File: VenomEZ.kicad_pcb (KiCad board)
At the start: 2 copper layers, 72 x 42 mm, 43 parts, among them CN1 HC-XH-5A-G, CN10 HC-XH-2A-G, CN2 HC-PH-8A-G, CN3 HC-XH-8A-G, CN4 HC-XH-8A-G, CN5 HC-XH-2A-G, CN6 HC-PH-7A-G, CN7 HC-XH-2A-G, CN8 HC-XH-2A-G, CN9 HC-XH-2A-G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

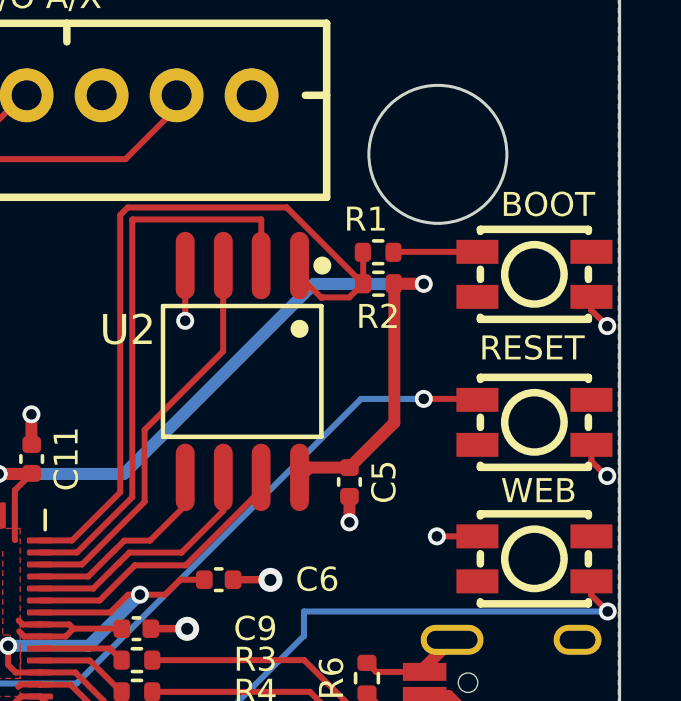
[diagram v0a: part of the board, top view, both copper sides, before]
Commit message: Move buttons and R1/R2 for better clearance around screw
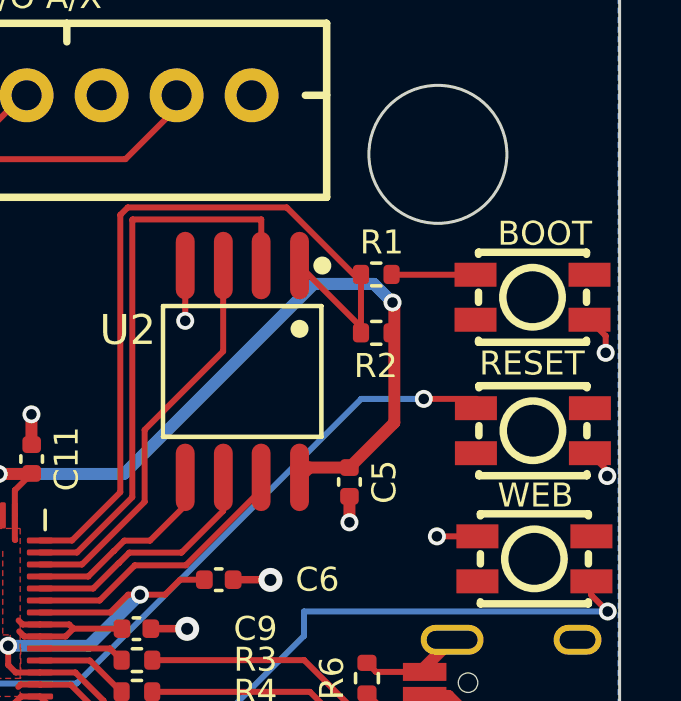
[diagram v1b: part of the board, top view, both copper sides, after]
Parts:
- moved R2 1.64 mm to (141.3, 86.7)
- moved SW3 0.77 mm to (146.6, 85.5)
- moved R1 0.74 mm to (141.3, 84.7)
- moved SW2 0.28 mm to (146.6, 89.9)
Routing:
- net +3V3: track 71.6 -> 69.2 mm
- net QSPI_SS: track 25.9 -> 26.5 mm

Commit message: 1.2
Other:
- board text added: "Version 1.2 Powered by GP2040-CE"
- board text removed: "Version 1.1 Powered by GP2040-CE"
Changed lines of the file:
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@@
     (effects (font (size 0.8 0.8) (thickness 0.15)) (justify left bottom))
   )
-  (gr_text "Version 1.1\nPowered by GP2040-CE" (at 96.396823 90.614668) (layer "F.SilkS")
+  (gr_text "Version 1.2\nPowered by GP2040-CE" (at 96.396823 90.614668) (layer "F.SilkS")
     (effects (font (size 1 1) (thickness 0.09)) (justify left bottom))
   )

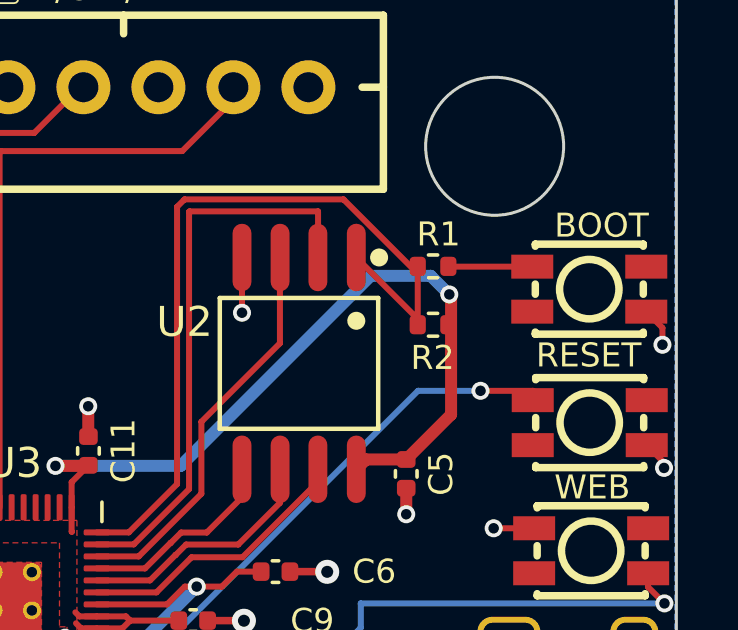
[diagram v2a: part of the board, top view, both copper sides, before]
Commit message: Move R1 and R2 closer together
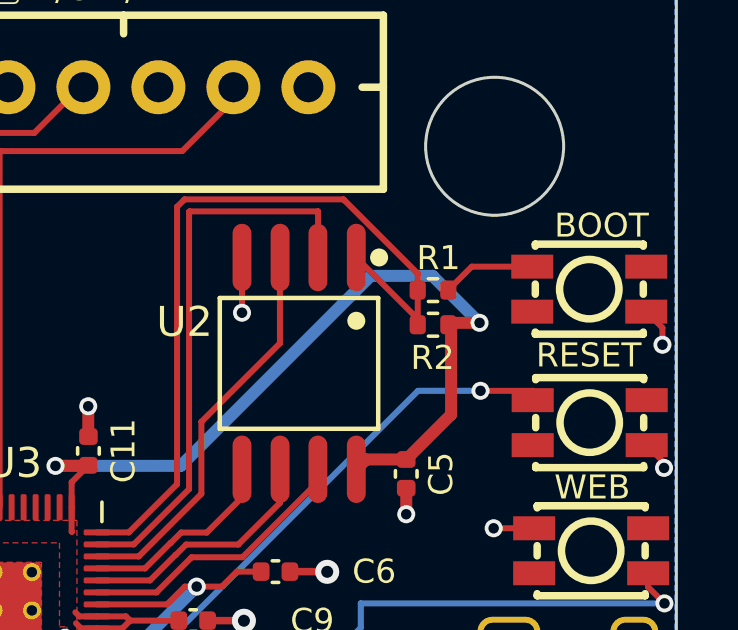
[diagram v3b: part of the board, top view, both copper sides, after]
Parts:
- moved R1 0.79 mm to (141.3, 85.5)
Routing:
- net +3V3: track 69.2 -> 70.7 mm
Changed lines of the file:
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@@
   )
   (footprint "Resistor_SMD:R_0402_1005Metric" (layer "F.Cu")
-    (at 141.348354 84.711995)
+    (at 141.347237 85.502328)
     (descr "Resistor SMD 0402 (1005 Metric), square (rectangular) end terminal, IPC_7351 nominal, (Body size source: IPC-SM-782 page 72, https://www.pcb-3d.com/wordpress/wp-content/uploads/ipc-sm-782a_amendment_1_and_2.pdf), generated with kicad-footprint-generator")
     (tags "resistor")
@@
   (segment (start 129.30151 98.990949) (end 129.512459 98.78) (width 0.2) (layer "F.Cu") (net 34))
   (segment (start 129.30151 93.552748) (end 129.313254 93.564492) (width 0.2) (layer "F.Cu") (net 34))
-  (segment (start 141.950201 85.707586) (end 141.890251 85.647636) (width 0.4) (layer "F.Cu") (net 34))
   (segment (start 129.844008 91.362421) (end 129.861793 91.344636) (width 0.2) (layer "F.Cu") (net 34))
   (segment (start 129.30151 92.7425) (end 129.30151 91.904919) (width 0.2) (layer "F.Cu") (net 34))
@@
   (segment (start 130.13901 98.38) (end 130.145139 98.386129) (width 0.2) (layer "F.Cu") (net 34))
   (segment (start 131.113273 96.38) (end 130.13901 96.38) (width 0.2) (layer "F.Cu") (net 34))
+  (segment (start 140.454685 91.148537) (end 141.950201 89.653021) (width 0.4) (layer "F.Cu") (net 34))
   (segment (start 129.30151 99.6175) (end 129.30151 98.990949) (width 0.2) (layer "F.Cu") (net 34))
   (segment (start 134.847542 106.924702) (end 135.041033 106.924702) (width 0.4) (layer "F.Cu") (net 34))
+  (segment (start 141.950201 89.653021) (end 141.950201 86.749551) (width 0.4) (layer "F.Cu") (net 34))
   (segment (start 129.30151 92.7425) (end 129.30151 93.552748) (width 0.2) (layer "F.Cu") (net 34))
   (segment (start 125.70151 92.7425) (end 125.70151 91.022448) (width 0.2) (layer "F.Cu") (net 34))
@@
   (segment (start 129.512459 98.78) (end 130.13901 98.78) (width 0.2) (layer "F.Cu") (net 34))
   (segment (start 122.05412 96.38) (end 123.26401 96.38) (width 0.2) (layer "F.Cu") (net 34))
-  (segment (start 141.950201 89.653021) (end 141.950201 85.707586) (width 0.4) (layer "F.Cu") (net 34))
   (segment (start 131.252393 96.51912) (end 130.991513 96.78) (width 0.2) (layer "F.Cu") (net 34))
   (segment (start 119.740309 106.064071) (end 120.28447 106.064071) (width 0.2) (layer "F.Cu") (net 34))
   (segment (start 135.057663 106.908072) (end 135.041033 106.924702) (width 0.2) (layer "F.Cu") (net 34))
   (segment (start 124.03519 96.38) (end 124.043381 96.388191) (width 0.2) (layer "F.Cu") (net 34))
+  (segment (start 141.922148 86.59391) (end 141.858354 86.657704) (width 0.4) (layer "F.Cu") (net 34))
   (segment (start 131.159352 98.386129) (end 131.857521 99.084298) (width 0.2) (layer "F.Cu") (net 34))
+  (segment (start 142.899201 86.59391) (end 141.922148 86.59391) (width 0.4) (layer "F.Cu") (net 34))
   (segment (start 131.857521 103.934681) (end 134.847542 106.924702) (width 0.4) (layer "F.Cu") (net 34))
   (segment (start 130.991513 96.78) (end 130.13901 96.78) (width 0.2) (layer "F.Cu") (net 34))
@@
   (segment (start 128.763082 91.362421) (end 129.844008 91.362421) (width 0.4) (layer "F.Cu") (net 34))
   (segment (start 131.857521 99.084298) (end 131.857521 100.711465) (width 0.2) (layer "F.Cu") (net 34))
+  (segment (start 141.950201 86.749551) (end 141.858354 86.657704) (width 0.4) (layer "F.Cu") (net 34))
   (segment (start 125.70151 99.6175) (end 125.70151 99.085025) (width 0.2) (layer "F.Cu") (net 34))
   (segment (start 129.617561 96.78) (end 129.446174 96.608613) (width 0.2) (layer "F.Cu") (net 34))
-  (segment (start 140.454685 91.148537) (end 141.950201 89.653021) (width 0.4) (layer "F.Cu") (net 34))
   (segment (start 130.13901 96.78) (end 129.617561 96.78) (width 0.2) (layer "F.Cu") (net 34))
   (segment (start 129.561589 96.38) (end 129.425324 96.243735) (width 0.2) (layer "F.Cu") (net 34))
   (segment (start 125.70151 91.022448) (end 125.43422 90.755158) (width 0.2) (layer "F.Cu") (net 34))
   (via (at 128.763082 91.362421) (size 0.6) (drill 0.35) (layers "F.Cu" "B.Cu") (free) (net 34))
-  (via (at 141.890251 85.647636) (size 0.6) (drill 0.35) (layers "F.Cu" "B.Cu") (free) (net 34))
+  (via (at 142.899201 86.59391) (size 0.6) (drill 0.35) (layers "F.Cu" "B.Cu") (free) (net 34))
   (segment (start 139.270815 85.027118) (end 132.935512 91.362421) (width 0.4) (layer "B.Cu") (net 34))
-  (segment (start 141.890251 85.647636) (end 141.269733 85.027118) (width 0.4) (layer "B.Cu") (net 34))
-  (segment (start 141.269733 85.027118) (end 139.270815 85.027118) (width 0.4) (layer "B.Cu") (net 34))
+  (segment (start 141.332409 85.027118) (end 139.270815 85.027118) (width 0.4) (layer "B.Cu") (net 34))
   (segment (start 132.935512 91.362421) (end 128.763082 91.362421) (width 0.4) (layer "B.Cu") (net 34))
+  (segment (start 142.899201 86.59391) (end 141.332409 85.027118) (width 0.4) (layer "B.Cu") (net 34))
   (segment (start 117.807657 95.133875) (end 118.253782 95.58) (width 0.2) (layer "F.Cu") (net 35))
   (segment (start 118.253782 95.58) (end 123.26401 95.58) (width 0.2) (layer "F.Cu") (net 35))
@@
   (segment (start 132.815831 82.727378) (end 132.815831 91.970701) (width 0.2) (layer "F.Cu") (net 42))
   (segment (start 131.206532 93.58) (end 130.13901 93.58) (width 0.2) (layer "F.Cu") (net 42))
-  (segment (start 144.656611 84.721509) (end 141.867868 84.721509) (width 0.2) (layer "F.Cu") (net 43))
-  (segment (start 141.867868 84.721509) (end 141.858354 84.711995) (width 0.2) (layer "F.Cu") (net 43))
+  (segment (start 142.638056 84.721509) (end 141.857237 85.502328) (width 0.2) (layer "F.Cu") (net 43))
+  (segment (start 144.656611 84.721509) (end 142.638056 84.721509) (width 0.2) (layer "F.Cu") (net 43))
   (segment (start 133.29924 94.408514) (end 132.127754 95.58) (width 0.2) (layer "F.Cu") (net 46))
   (segment (start 137.515259 91.890331) (end 134.997076 94.408514) (width 0.2) (layer "F.Cu") (net 46))

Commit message: Update silk for 1.3
(cherry picked from commit d50c346d8888544253aca363da94d46f0ae0f3f4)
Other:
- board text added: "Version 1.3 Powered by GP2040-CE"
- board text removed: "Version 1.2 Powered by GP2040-CE"
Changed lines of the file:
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@@
     (effects (font (size 0.8 0.8) (thickness 0.15)) (justify left bottom))
   )
-  (gr_text "Version 1.2\nPowered by GP2040-CE" (at 96.396823 90.614668) (layer "F.SilkS")
+  (gr_text "Version 1.3\nPowered by GP2040-CE" (at 96.396823 90.614668) (layer "F.SilkS")
     (effects (font (size 1 1) (thickness 0.09)) (justify left bottom))
   )

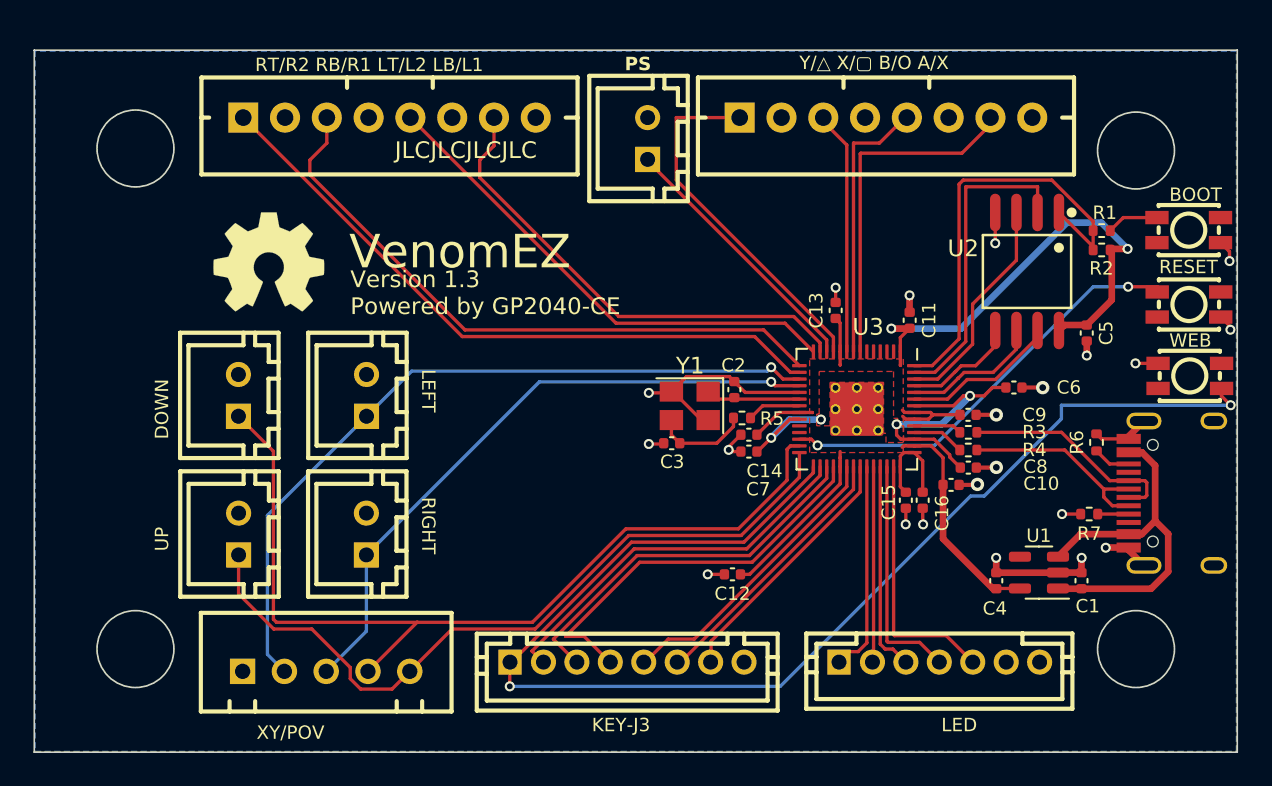
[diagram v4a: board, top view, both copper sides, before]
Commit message: Started og usb connector / redesign
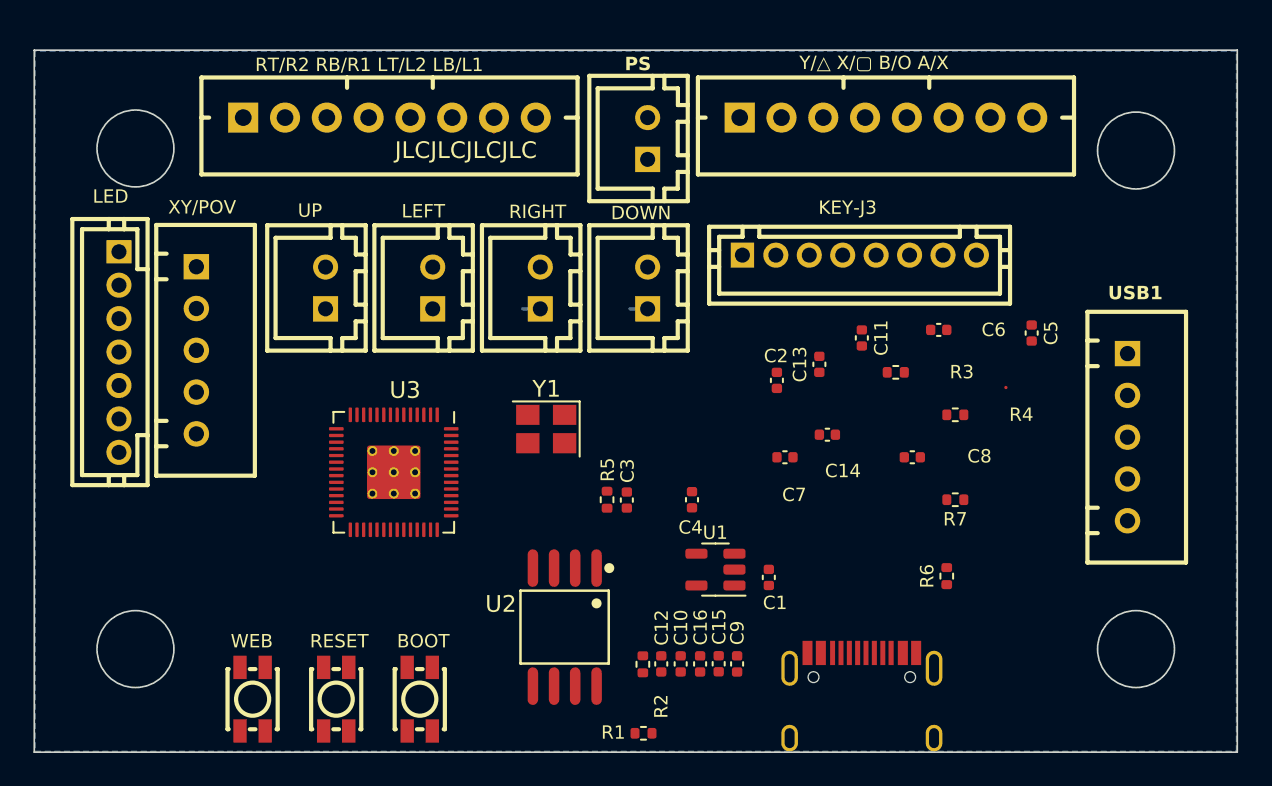
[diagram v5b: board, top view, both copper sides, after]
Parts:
- removed OSHW1: OSHW-Symbol_6.7x6mm_SilkScreen, Symbol:OSHW-Symbol_6.7x6mm_SilkScreen
- added CN11: HC-XH-5A-G, easyeda2kicad:CONN-TH_5P-P2.50_HC-XH-5A-G, F.Cu at (142.9, 97.9)
- moved SW1 59.3 mm to (90.6, 113.5), turned to -90 degrees
- moved SW2 56.2 mm to (95.6, 113.5), turned to -90 degrees
- moved SW3 53.9 mm to (100.6, 113.5), turned to -90 degrees
- moved CN6 52.5 mm to (82.6, 92.8), turned to -90 degrees
- moved R1 40.7 mm to (113.9, 115.6), turned to 180 degrees
- moved R2 37.0 mm to (113.9, 111.4), turned to 90 degrees
- moved U2 34.9 mm to (109.2, 109.2)
- moved USB1 29.3 mm to (127.0, 118.5), turned to 0 degrees
- moved CN2 28.0 mm to (126.9, 87.0)
- moved U3 28.0 mm to (99.0, 100.0)
- moved CN10 25.3 mm to (114.2, 88.9)
- moved CN1 20.7 mm to (87.2, 92.7), turned to -90 degrees
- moved C9 20.3 mm to (119.5, 111.4), turned to 90 degrees
- moved C10 19.4 mm to (116.2, 111.4), turned to 90 degrees
- moved U1 19.4 mm to (118.2, 105.8)
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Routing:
- net S2 (START): track 76.5 -> 0.00 mm, vias 2 -> 0
- net +3V3: track 70.7 -> 0.00 mm, vias 2 -> 0
- net DOWN: track 54.2 -> 1.05 mm
- net GND: track 45.9 -> 0.00 mm, vias 21 -> 0
- net UP: track 45.4 -> 0.00 mm
- net LEFT: track 45.5 -> 0.53 mm, vias 1 -> 0
- net (3K) R2: track 39.6 -> 0.00 mm
- net (3P) R1: track 37.9 -> 0.00 mm
- net RIGHT: track 38.3 -> 1.05 mm, vias 1 -> 0
- net (4K) L2: track 29.9 -> 0.00 mm
- net (4P) L1: track 28.9 -> 1.69 mm
- net QSPI_SS: track 26.5 -> 0.00 mm
- net RUN: track 25.6 -> 0.00 mm, vias 2 -> 0
- net TURBO: track 24.1 -> 0.00 mm
- net +1V1: track 23.1 -> 0.00 mm, vias 4 -> 0
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- removed copper zone on F.Cu, net +1V1
- removed copper zone on F.Cu, net +3V3
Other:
- board text added: "USB1"
- board text removed: "VenomEZ"
- board text removed: "Version 1.3 Powered by GP2040-CE"

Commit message: Very wip
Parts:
- removed G***: LOGO, GP2040-CE:gp2040-ce-logo
- moved C14 31.5 mm to (94.5, 105.7)
- moved C2 30.2 mm to (92.9, 102.9)
- moved C7 29.0 mm to (94.5, 106.7)
- moved R4 27.4 mm to (108.1, 108.8)
- moved C6 27.1 mm to (108.1, 105.0)
- moved C13 25.2 mm to (99.9, 99.1)
- moved R3 25.0 mm to (108.1, 107.7)
- moved C3 24.9 mm to (88.8, 107.7), turned to 180 degrees
- moved C8 24.4 mm to (108.2, 109.8)
- moved C11 24.0 mm to (104.1, 99.1)
- moved C5 22.4 mm to (118.6, 104.1)
- moved R1 19.9 mm to (119.8, 96.6), turned to 0 degrees
- moved Y1 19.7 mm to (90.0, 105.0)
- moved R5 18.0 mm to (94.0, 104.7), turned to 0 degrees
- moved C12 16.7 mm to (98.3, 110.4), turned to -90 degrees
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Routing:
- net +3V3: track 0.00 -> 110.8 mm
- net GND: track 0.00 -> 55.2 mm, vias 0 -> 18
- net +5V: track 0.00 -> 49.6 mm, vias 0 -> 1
- net D+: track 0.00 -> 45.2 mm, vias 0 -> 2
- net D-: track 0.00 -> 43.3 mm, vias 0 -> 2
- net S2 (START): track 0.00 -> 40.8 mm, vias 0 -> 1
- net DOWN: track 1.05 -> 29.1 mm
- net BOOTSEL: track 0.00 -> 26.2 mm, vias 0 -> 2
- net QSPI_SS: track 0.00 -> 25.7 mm
- net RIGHT: track 1.05 -> 21.6 mm
- net QSPI_SD1: track 0.00 -> 20.1 mm
- net QSPI_SD2: track 0.00 -> 14.7 mm
- net LEFT: track 0.53 -> 15.0 mm
- net QSPI_SD3: track 0.00 -> 12.9 mm
- net +1V1: track 0.00 -> 12.5 mm
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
